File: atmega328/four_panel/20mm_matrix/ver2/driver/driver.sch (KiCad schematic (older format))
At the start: 56 parts, among them IC1 ATMEGA328P-M, IC2 ATMEGA328P-M, IC3 ATMEGA328P-M, IC4 ATMEGA328P-M, X1 CER_RESO, X2 CER_RESO, X3 CER_RESO, X4 CER_RESO

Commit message: Worked on ver2 of atmega328 4x20mm driver and comm pcbs.
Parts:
- gave numbers to parts that had none: 4
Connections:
- net labels added: COL0_DRV0, COL0_DRV1, COL0_DRV2, COL0_DRV3, ROW0_DRV0, ROW0_DRV1, ROW0_DRV2, ROW0_DRV3
- net labels removed: COL8_DRV0, COL8_DRV1, COL8_DRV2, RESET_DRV4, ROW8_DRV0, ROW8_DRV1, ROW8_DRV2
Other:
- moved on the sheet: MATRIX1, MATRIX2, MATRIX3, MATRIX4, R10, R11, R12, R13, R14, R15, R16, R17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

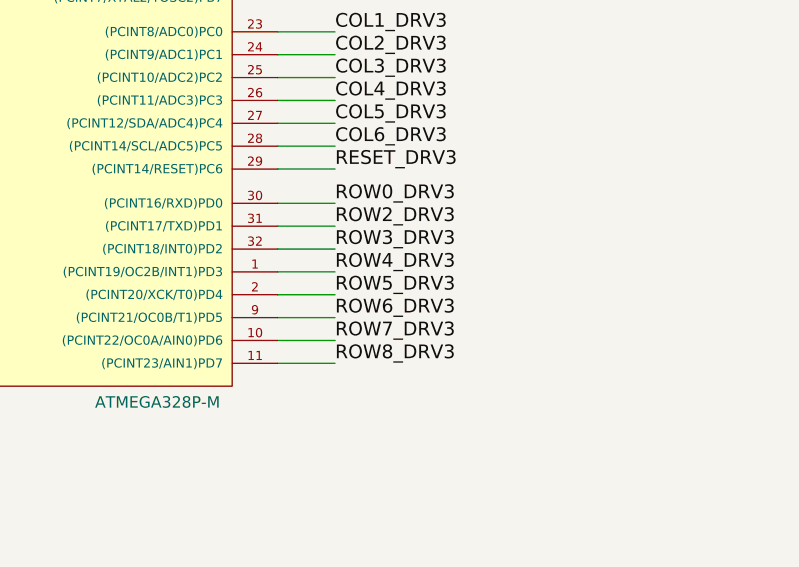
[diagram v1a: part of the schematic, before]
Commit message: Finished preliminary version 2.0 of atmega328 4x20mm panels design.
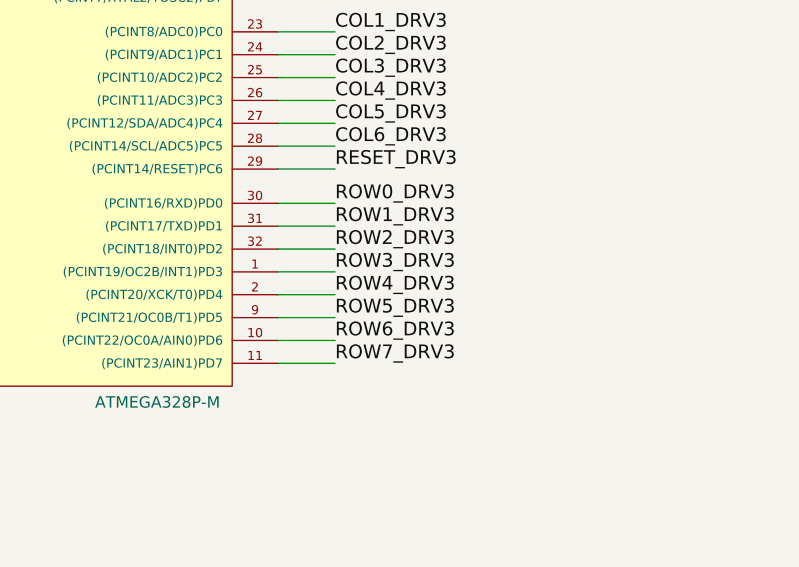
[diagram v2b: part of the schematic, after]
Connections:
- net ROW8_DRV3 is gone; now on net ROW7_DRV3: IC4.11 ((PCINT23/AIN1)PD7)
- net ROW1_DRV3: now also IC4.31 ((PCINT17/TXD)PD1)
- net ROW2_DRV3: now also IC4.32 ((PCINT18/INT0)PD2); no longer IC4.31 ((PCINT17/TXD)PD1)
- net ROW3_DRV3: now also IC4.1 ((PCINT19/OC2B/INT1)PD3); no longer IC4.32 ((PCINT18/INT0)PD2)
- net ROW4_DRV3: now also IC4.2 ((PCINT20/XCK/T0)PD4); no longer IC4.1 ((PCINT19/OC2B/INT1)PD3)
- net ROW5_DRV3: now also IC4.9 ((PCINT21/OC0B/T1)PD5); no longer IC4.2 ((PCINT20/XCK/T0)PD4)
- net ROW6_DRV3: now also IC4.10 ((PCINT22/OC0A/AIN0)PD6); no longer IC4.9 ((PCINT21/OC0B/T1)PD5)
- net ROW7_DRV3: no longer IC4.10 ((PCINT22/OC0A/AIN0)PD6)
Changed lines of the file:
@@
 	16250 4050 16500 4050
-Wire Wire Line
-	16250 4150 16500 4150
 Wire Wire Line
 	16250 4250 16500 4250
@@
 Wire Wire Line
 	16250 4750 16500 4750
+Wire Wire Line
+	16250 4150 16500 4150
 Text Label 16500 4050 0    60   ~ 0
 ROW0_DRV3
+Text Label 16500 4250 0    60   ~ 0
+ROW2_DRV3
+Text Label 16500 4350 0    60   ~ 0
+ROW3_DRV3
+Text Label 16500 4450 0    60   ~ 0
+ROW4_DRV3
+Text Label 16500 4550 0    60   ~ 0
+ROW5_DRV3
+Text Label 16500 4650 0    60   ~ 0
+ROW6_DRV3
+Text Label 16500 4750 0    60   ~ 0
+ROW7_DRV3
 Text Label 16500 4150 0    60   ~ 0
-ROW2_DRV3
-Text Label 16500 4250 0    60   ~ 0
-ROW3_DRV3
-Text Label 16500 4350 0    60   ~ 0
-ROW4_DRV3
-Text Label 16500 4450 0    60   ~ 0
-ROW5_DRV3
-Text Label 16500 4550 0    60   ~ 0
-ROW6_DRV3
-Text Label 16500 4650 0    60   ~ 0
-ROW7_DRV3
-Text Label 16500 4750 0    60   ~ 0
-ROW8_DRV3
+ROW1_DRV3
 Wire Wire Line
 	16250 3300 16500 3300

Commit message: Added some notes.
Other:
- note added: "Check matrix pinout !!!!"
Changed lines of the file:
@@
 NoConn ~ 5500 12300
 NoConn ~ 7500 12400
+Text Notes 7000 11200 0    300  ~ 0
+Check matrix pinout !!!!
 $EndSCHEMATC

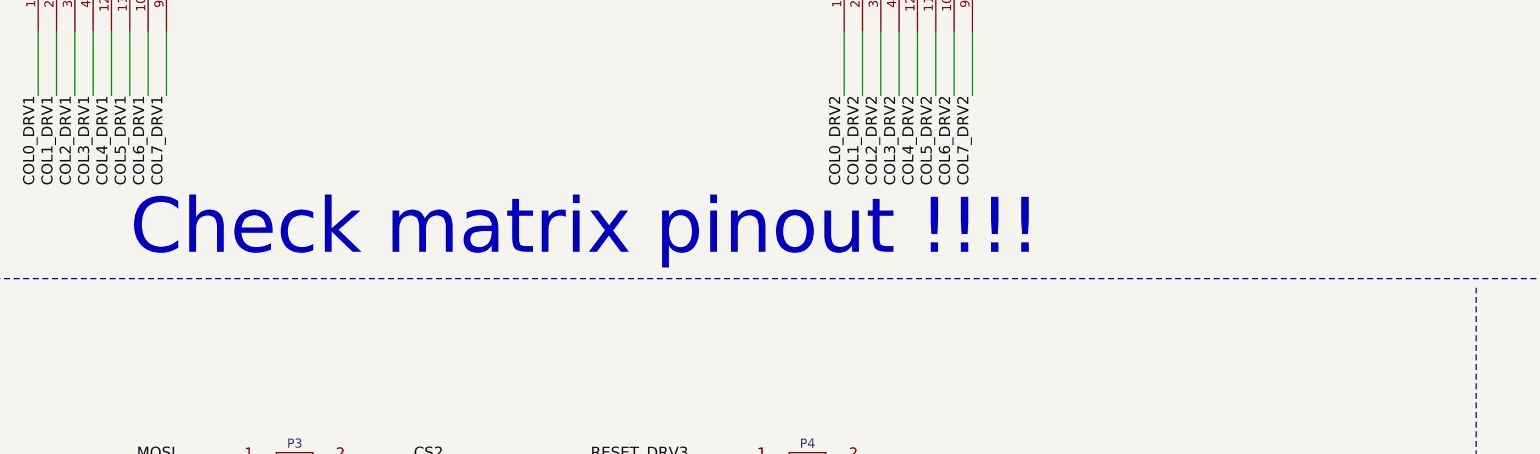
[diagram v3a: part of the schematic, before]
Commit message: Created gerber files for v0p2 of atmega328 4x20mm driver.
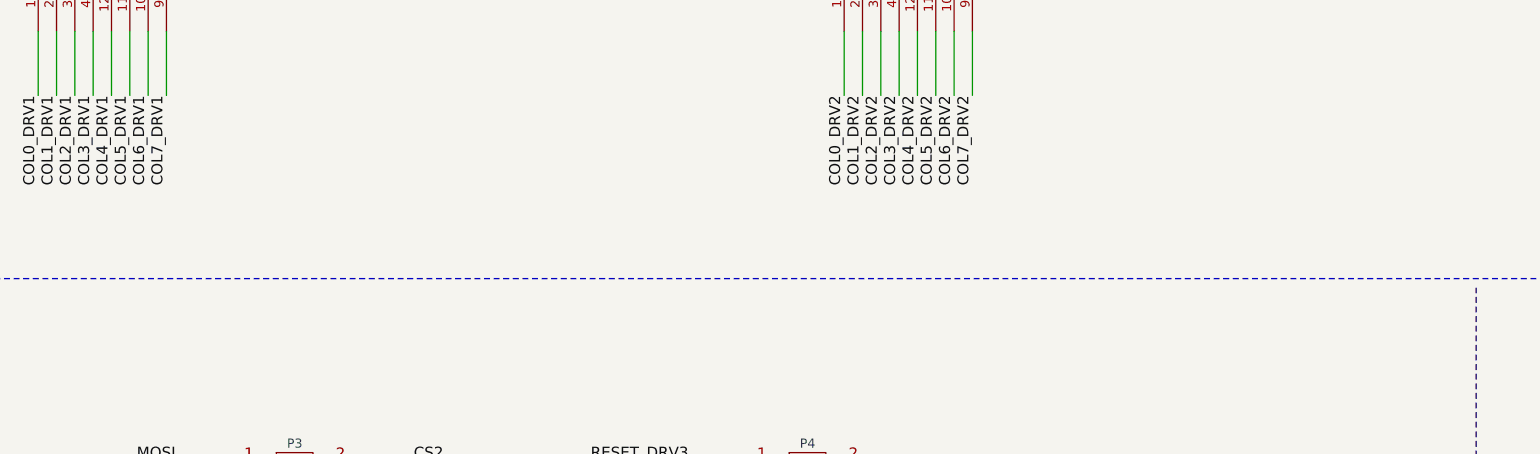
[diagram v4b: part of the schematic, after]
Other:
- note removed: "Check matrix pinout !!!!"
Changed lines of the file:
@@
 NoConn ~ 5500 12300
 NoConn ~ 7500 12400
-Text Notes 7000 11200 0    300  ~ 0
-Check matrix pinout !!!!
 $EndSCHEMATC

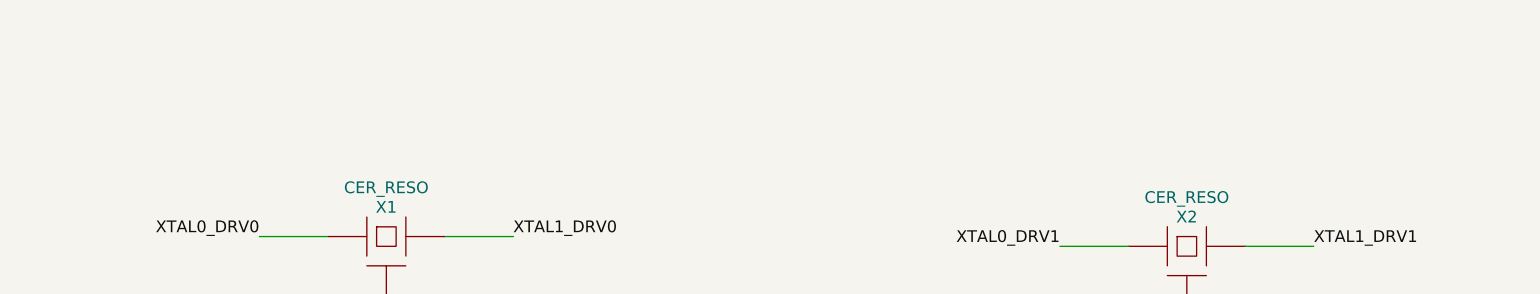
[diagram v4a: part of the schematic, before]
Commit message: Added notes to driver.  Boundary between revisions.
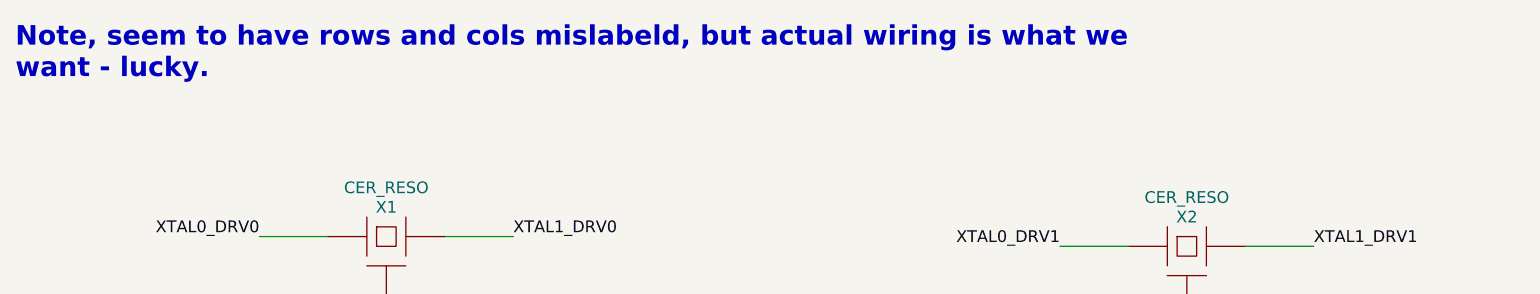
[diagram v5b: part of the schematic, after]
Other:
- note added: "Note, seem to have rows and cols mislabeld, but actual wiring is what we \nwant - lucky."
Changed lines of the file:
@@
 NoConn ~ 5500 12300
 NoConn ~ 7500 12400
+Text Notes 550  650  0    100  ~ 20
+Note, seem to have rows and cols mislabeld, but actual wiring is what we \nwant - lucky.
 $EndSCHEMATC

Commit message: Fixed error on 4-th driver in atmega328 4x20mm subpanel. Rerouted (preliminary). Still need to remake gerbers, update revision number, etc.
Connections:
- net COL8_DRV3 is gone; now on net ROW7_DRV3: IC4.13 ((PCINT1/OC1A)PB1)
- net COL0_DRV0: now also IC1.30 ((PCINT16/RXD)PD0), R5.1; no longer IC1.23 ((PCINT8/ADC0)PC0), MATRIX1.1 (C0)
- net COL0_DRV1: now also IC2.30 ((PCINT16/RXD)PD0), R13.1; no longer IC2.23 ((PCINT8/ADC0)PC0), MATRIX2.1 (C0)
- net COL0_DRV2: now also IC3.30 ((PCINT16/RXD)PD0), R21.1; no longer IC3.23 ((PCINT8/ADC0)PC0), MATRIX3.1 (C0)
- net COL0_DRV3: now also IC4.30 ((PCINT16/RXD)PD0), R29.1; no longer MATRIX4.1 (C0)
- net COL1_DRV0: now also IC1.31 ((PCINT17/TXD)PD1), R6.1; no longer IC1.24 ((PCINT9/ADC1)PC1), MATRIX1.2 (C1)
- net COL1_DRV1: now also IC2.31 ((PCINT17/TXD)PD1), R14.1; no longer IC2.24 ((PCINT9/ADC1)PC1), MATRIX2.2 (C1)
- net COL1_DRV2: now also IC3.31 ((PCINT17/TXD)PD1), R22.1; no longer IC3.24 ((PCINT9/ADC1)PC1), MATRIX3.2 (C1)
- net COL1_DRV3: now also IC4.31 ((PCINT17/TXD)PD1), R30.1; no longer IC4.23 ((PCINT8/ADC0)PC0), MATRIX4.2 (C1)
- net COL2_DRV0: now also IC1.32 ((PCINT18/INT0)PD2), R7.1; no longer IC1.25 ((PCINT10/ADC2)PC2), MATRIX1.3 (C2)
- net COL2_DRV1: now also IC2.32 ((PCINT18/INT0)PD2), R15.1; no longer IC2.25 ((PCINT10/ADC2)PC2), MATRIX2.3 (C2)
- net COL2_DRV2: now also IC3.32 ((PCINT18/INT0)PD2), R23.1; no longer IC3.25 ((PCINT10/ADC2)PC2), MATRIX3.3 (C2)
- net COL2_DRV3: now also IC4.32 ((PCINT18/INT0)PD2), R31.1; no longer IC4.24 ((PCINT9/ADC1)PC1), MATRIX4.3 (C2)
- net COL3_DRV0: now also IC1.1 ((PCINT19/OC2B/INT1)PD3), R8.1; no longer IC1.26 ((PCINT11/ADC3)PC3), MATRIX1.4 (C3)
- net COL3_DRV1: now also IC2.1 ((PCINT19/OC2B/INT1)PD3), R16.1; no longer IC2.26 ((PCINT11/ADC3)PC3), MATRIX2.4 (C3)
- net COL3_DRV2: now also IC3.1 ((PCINT19/OC2B/INT1)PD3), R24.1; no longer IC3.26 ((PCINT11/ADC3)PC3), MATRIX3.4 (C3)
- net COL3_DRV3: now also IC4.1 ((PCINT19/OC2B/INT1)PD3), R32.1; no longer IC4.25 ((PCINT10/ADC2)PC2), MATRIX4.4 (C3)
- net COL4_DRV0: now also IC1.2 ((PCINT20/XCK/T0)PD4), R9.1; no longer IC1.27 ((PCINT12/SDA/ADC4)PC4), MATRIX1.12 (C4)
- net COL4_DRV1: now also IC2.2 ((PCINT20/XCK/T0)PD4), R17.1; no longer IC2.27 ((PCINT12/SDA/ADC4)PC4), MATRIX2.12 (C4)
- net COL4_DRV2: now also IC3.2 ((PCINT20/XCK/T0)PD4), R25.1; no longer IC3.27 ((PCINT12/SDA/ADC4)PC4), MATRIX3.12 (C4)
- net COL4_DRV3: now also IC4.2 ((PCINT20/XCK/T0)PD4), R33.1; no longer IC4.26 ((PCINT11/ADC3)PC3), MATRIX4.12 (C4)
- net COL5_DRV0: now also IC1.9 ((PCINT21/OC0B/T1)PD5), R10.1; no longer IC1.28 ((PCINT14/SCL/ADC5)PC5), MATRIX1.11 (C5)
- net COL5_DRV1: now also IC2.9 ((PCINT21/OC0B/T1)PD5), R18.1; no longer IC2.28 ((PCINT14/SCL/ADC5)PC5), MATRIX2.11 (C5)
- net COL5_DRV2: now also IC3.9 ((PCINT21/OC0B/T1)PD5), R26.1; no longer IC3.28 ((PCINT14/SCL/ADC5)PC5), MATRIX3.11 (C5)
- net COL5_DRV3: now also IC4.9 ((PCINT21/OC0B/T1)PD5), R34.1; no longer IC4.27 ((PCINT12/SDA/ADC4)PC4), MATRIX4.11 (C5)
- net COL6_DRV0: now also IC1.10 ((PCINT22/OC0A/AIN0)PD6), R11.1; no longer IC1.12 ((PCINT0/CLKO/ICP1)PB0), MATRIX1.10 (C6)
- net COL6_DRV1: now also IC2.10 ((PCINT22/OC0A/AIN0)PD6), R19.1; no longer IC2.12 ((PCINT0/CLKO/ICP1)PB0), MATRIX2.10 (C6)
- net COL6_DRV2: now also IC3.10 ((PCINT22/OC0A/AIN0)PD6), R27.1; no longer IC3.12 ((PCINT0/CLKO/ICP1)PB0), MATRIX3.10 (C6)
- net COL6_DRV3: now also IC4.10 ((PCINT22/OC0A/AIN0)PD6), R35.1; no longer IC4.28 ((PCINT14/SCL/ADC5)PC5), MATRIX4.10 (C6)
- net COL7_DRV0: now also IC1.11 ((PCINT23/AIN1)PD7), R12.1; no longer IC1.13 ((PCINT1/OC1A)PB1), MATRIX1.9 (C7)
- net COL7_DRV1: now also IC2.11 ((PCINT23/AIN1)PD7), R20.1; no longer IC2.13 ((PCINT1/OC1A)PB1), MATRIX2.9 (C7)
- net COL7_DRV2: now also IC3.11 ((PCINT23/AIN1)PD7), R28.1; no longer IC3.13 ((PCINT1/OC1A)PB1), MATRIX3.9 (C7)
- net COL7_DRV3: now also IC4.11 ((PCINT23/AIN1)PD7), R36.1; no longer IC4.12 ((PCINT0/CLKO/ICP1)PB0), MATRIX4.9 (C7)
- net ROW0_DRV0: now also IC1.23 ((PCINT8/ADC0)PC0), MATRIX1.1 (C0); no longer IC1.30 ((PCINT16/RXD)PD0), R5.1
- net ROW0_DRV1: now also IC2.23 ((PCINT8/ADC0)PC0), MATRIX2.1 (C0); no longer IC2.30 ((PCINT16/RXD)PD0), R13.1
- net ROW0_DRV2: now also IC3.23 ((PCINT8/ADC0)PC0), MATRIX3.1 (C0); no longer IC3.30 ((PCINT16/RXD)PD0), R21.1
- net ROW0_DRV3: now also IC4.23 ((PCINT8/ADC0)PC0), MATRIX4.1 (C0); no longer IC4.30 ((PCINT16/RXD)PD0), R29.1
- net ROW1_DRV0: now also IC1.24 ((PCINT9/ADC1)PC1), MATRIX1.2 (C1); no longer IC1.31 ((PCINT17/TXD)PD1), R6.1
- net ROW1_DRV1: now also IC2.24 ((PCINT9/ADC1)PC1), MATRIX2.2 (C1); no longer IC2.31 ((PCINT17/TXD)PD1), R14.1
- net ROW1_DRV2: now also IC3.24 ((PCINT9/ADC1)PC1), MATRIX3.2 (C1); no longer IC3.31 ((PCINT17/TXD)PD1), R22.1
- net ROW1_DRV3: now also IC4.24 ((PCINT9/ADC1)PC1), MATRIX4.2 (C1); no longer IC4.31 ((PCINT17/TXD)PD1), R30.1
- net ROW2_DRV0: now also IC1.25 ((PCINT10/ADC2)PC2), MATRIX1.3 (C2); no longer IC1.32 ((PCINT18/INT0)PD2), R7.1
- net ROW2_DRV1: now also IC2.25 ((PCINT10/ADC2)PC2), MATRIX2.3 (C2); no longer IC2.32 ((PCINT18/INT0)PD2), R15.1
- net ROW2_DRV2: now also IC3.25 ((PCINT10/ADC2)PC2), MATRIX3.3 (C2); no longer IC3.32 ((PCINT18/INT0)PD2), R23.1
- net ROW2_DRV3: now also IC4.25 ((PCINT10/ADC2)PC2), MATRIX4.3 (C2); no longer IC4.32 ((PCINT18/INT0)PD2), R31.1
- net ROW3_DRV0: now also IC1.26 ((PCINT11/ADC3)PC3), MATRIX1.4 (C3); no longer IC1.1 ((PCINT19/OC2B/INT1)PD3), R8.1
- net ROW3_DRV1: now also IC2.26 ((PCINT11/ADC3)PC3), MATRIX2.4 (C3); no longer IC2.1 ((PCINT19/OC2B/INT1)PD3), R16.1
- net ROW3_DRV2: now also IC3.26 ((PCINT11/ADC3)PC3), MATRIX3.4 (C3); no longer IC3.1 ((PCINT19/OC2B/INT1)PD3), R24.1
- net ROW3_DRV3: now also IC4.26 ((PCINT11/ADC3)PC3), MATRIX4.4 (C3); no longer IC4.1 ((PCINT19/OC2B/INT1)PD3), R32.1
- net ROW4_DRV0: now also IC1.27 ((PCINT12/SDA/ADC4)PC4), MATRIX1.12 (C4); no longer IC1.2 ((PCINT20/XCK/T0)PD4), R9.1
- net ROW4_DRV1: now also IC2.27 ((PCINT12/SDA/ADC4)PC4), MATRIX2.12 (C4); no longer IC2.2 ((PCINT20/XCK/T0)PD4), R17.1
- net ROW4_DRV2: now also IC3.27 ((PCINT12/SDA/ADC4)PC4), MATRIX3.12 (C4); no longer IC3.2 ((PCINT20/XCK/T0)PD4), R25.1
- net ROW4_DRV3: now also IC4.27 ((PCINT12/SDA/ADC4)PC4), MATRIX4.12 (C4); no longer IC4.2 ((PCINT20/XCK/T0)PD4), R33.1
- net ROW5_DRV0: now also IC1.28 ((PCINT14/SCL/ADC5)PC5), MATRIX1.11 (C5); no longer IC1.9 ((PCINT21/OC0B/T1)PD5), R10.1
- net ROW5_DRV1: now also IC2.28 ((PCINT14/SCL/ADC5)PC5), MATRIX2.11 (C5); no longer IC2.9 ((PCINT21/OC0B/T1)PD5), R18.1
- net ROW5_DRV2: now also IC3.28 ((PCINT14/SCL/ADC5)PC5), MATRIX3.11 (C5); no longer IC3.9 ((PCINT21/OC0B/T1)PD5), R26.1
- net ROW5_DRV3: now also IC4.28 ((PCINT14/SCL/ADC5)PC5), MATRIX4.11 (C5); no longer IC4.9 ((PCINT21/OC0B/T1)PD5), R34.1
- net ROW6_DRV0: now also IC1.12 ((PCINT0/CLKO/ICP1)PB0), MATRIX1.10 (C6); no longer IC1.10 ((PCINT22/OC0A/AIN0)PD6), R11.1
- net ROW6_DRV1: now also IC2.12 ((PCINT0/CLKO/ICP1)PB0), MATRIX2.10 (C6); no longer IC2.10 ((PCINT22/OC0A/AIN0)PD6), R19.1
- net ROW6_DRV2: now also IC3.12 ((PCINT0/CLKO/ICP1)PB0), MATRIX3.10 (C6); no longer IC3.10 ((PCINT22/OC0A/AIN0)PD6), R27.1
- net ROW6_DRV3: now also IC4.12 ((PCINT0/CLKO/ICP1)PB0), MATRIX4.10 (C6); no longer IC4.10 ((PCINT22/OC0A/AIN0)PD6), R35.1
- net ROW7_DRV0: now also IC1.13 ((PCINT1/OC1A)PB1), MATRIX1.9 (C7); no longer IC1.11 ((PCINT23/AIN1)PD7), R12.1
- net ROW7_DRV1: now also IC2.13 ((PCINT1/OC1A)PB1), MATRIX2.9 (C7); no longer IC2.11 ((PCINT23/AIN1)PD7), R20.1
- net ROW7_DRV2: now also IC3.13 ((PCINT1/OC1A)PB1), MATRIX3.9 (C7); no longer IC3.11 ((PCINT23/AIN1)PD7), R28.1
- net ROW7_DRV3: now also MATRIX4.9 (C7); no longer IC4.11 ((PCINT23/AIN1)PD7), R36.1
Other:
- note removed: "Note, seem to have rows and cols mislabeld, but actual wiring is what we \nwant - lucky."

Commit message: Added gerbers for driver.
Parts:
- R1, R2, R3, R4: value 1k -> 4.7k
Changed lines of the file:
@@
 P 1100 2500
 F 0 "R1" V 1180 2500 40  0000 C CNN
-F 1 "1k" V 1107 2501 40  0000 C CNN
+F 1 "4.7k" V 1107 2501 40  0000 C CNN
 F 2 "" V 1030 2500 30  0000 C CNN
 F 3 "" H 1100 2500 30  0000 C CNN
@@
 P 5400 2500
 F 0 "R2" V 5480 2500 40  0000 C CNN
-F 1 "1k" V 5407 2501 40  0000 C CNN
+F 1 "4.7k" V 5407 2501 40  0000 C CNN
 F 2 "" V 5330 2500 30  0000 C CNN
 F 3 "" H 5400 2500 30  0000 C CNN
@@
 P 9800 2500
 F 0 "R3" V 9880 2500 40  0000 C CNN
-F 1 "1k" V 9807 2501 40  0000 C CNN
+F 1 "4.7k" V 9807 2501 40  0000 C CNN
 F 2 "" V 9730 2500 30  0000 C CNN
 F 3 "" H 9800 2500 30  0000 C CNN
@@
 P 13950 2500
 F 0 "R4" V 14030 2500 40  0000 C CNN
-F 1 "1k" V 13957 2501 40  0000 C CNN
+F 1 "4.7k" V 13957 2501 40  0000 C CNN
 F 2 "" V 13880 2500 30  0000 C CNN
 F 3 "" H 13950 2500 30  0000 C CNN
